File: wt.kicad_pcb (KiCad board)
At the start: 4 copper layers, 70.9 x 100 mm, 181 parts, among them J1 USB_B, J2 Conn_ARM_JTAG_SWD_10, SW1 SW_Push, SW2 SW_Push, SW3 SW_Push, SW4 SW_Push, SW5 SW_Push, SW6 SW_Push, U1 LM324, U10 LUM-1502-03_3.5mm_mono_vertic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, U11 LUM-1502-03_3.5mm_mono_vertic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, U12 LUM-1502-03_3.5mm_mono_vertic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, U13 LUM-1502-03_3.5mm_mono_vertic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, U14 LUM-1502-03_3.5mm_mono_vertic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, U15 LUM-1502-03_3.5mm_mono_vertic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, U16 power_conn_10, U17 REF191, U18 L78L05ACU, U19 ZLDO1117G33TA, U2 LM324, U20 TL072, U21 LUM-1502-03_3.5mm_mono_vertic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, U22 LUM-1502-03_3.5mm_mono_vertic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, U23 LUM-1502-03_3.5mm_mono_vertic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, U24 LUM-1502-03_3.5mm_mono_vertic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, U3 LM324, U4 STM32F407VGTx, U5 TL074, U6 TL074, U7 TLC7528, U8 LUM-1502-03_3.5mm_mono_vertic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, U9 LUM-1502-03_3.5mm_mono_vertic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, Y1 Crystal_8Mhz

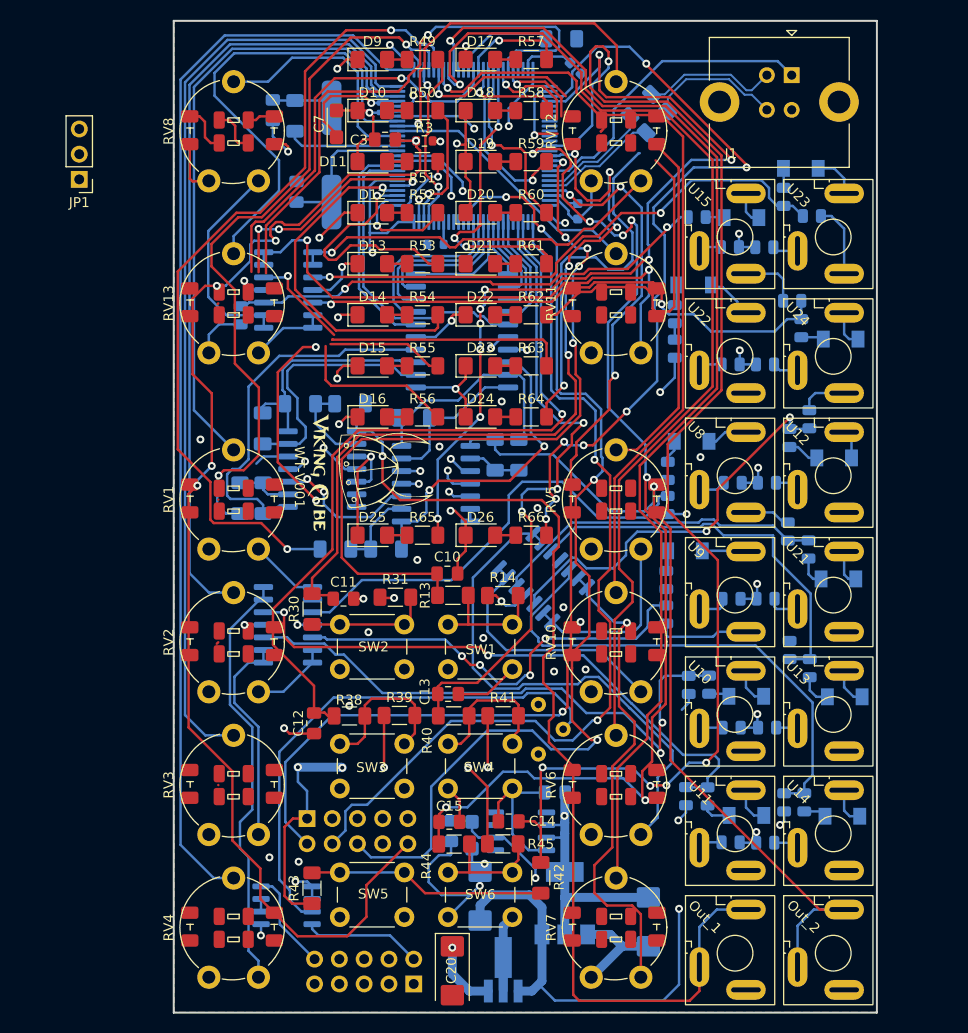
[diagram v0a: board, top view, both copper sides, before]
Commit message: fixed issues, power still needs to be addressed
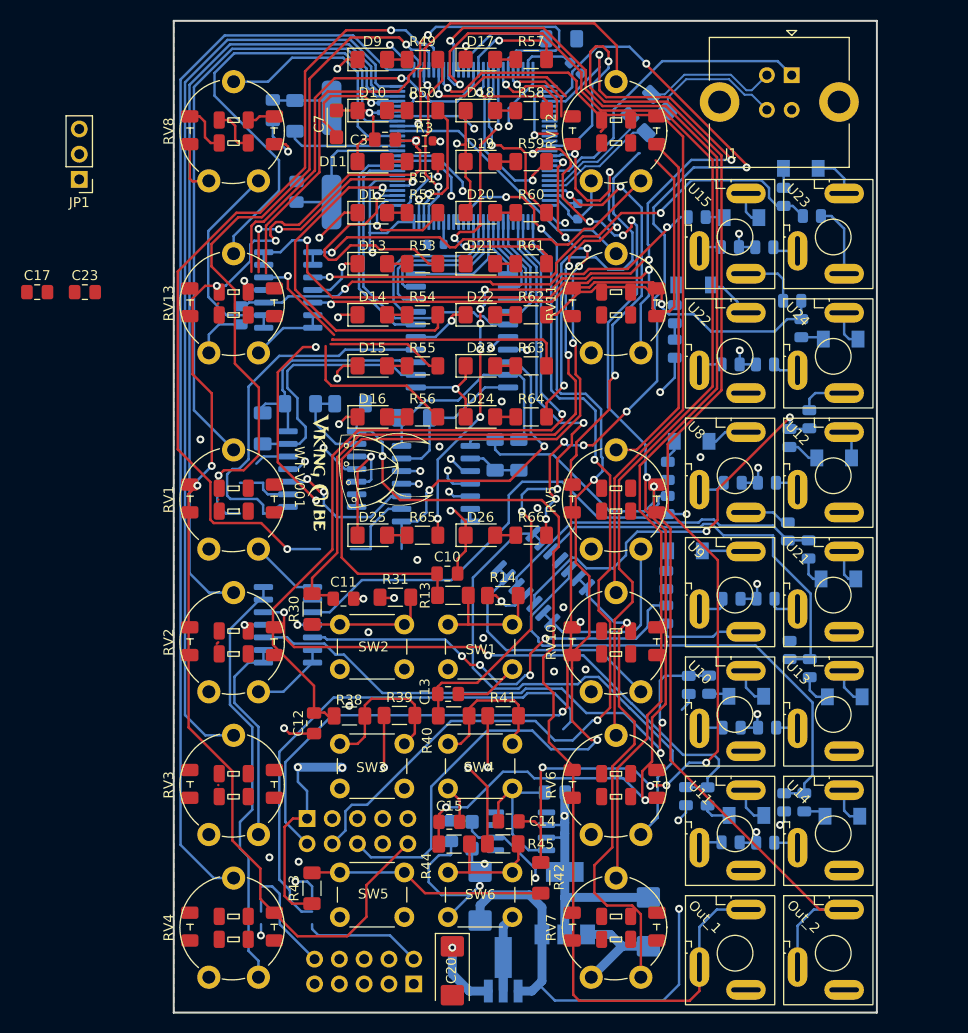
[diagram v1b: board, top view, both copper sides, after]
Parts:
- removed R5, R6, R7, R8: R-10k-1206, Resistor_SMD:R_1206_3216Metric_Pad1.30x1.75mm_HandSolder
- removed RV9: Trim_5k_prec_tht, eurorack:trim_2.5mm
- removed U20: TL072, Package_SO:SO-8_3.9x4.9mm_P1.27mm
- added C17: C-100nF-0805, Capacitor_SMD:C_0805_2012Metric_Pad1.18x1.45mm_HandSolder, F.Cu at (-13.8, 27.4)
- added C23: C-100nF-0805, Capacitor_SMD:C_0805_2012Metric_Pad1.18x1.45mm_HandSolder, F.Cu at (-8.96, 27.4)
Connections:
- R10 pad 1: Net-(C8-Pad2) -> Net-(R10-Pad1)
- R9 pad 1: Net-(C9-Pad1) -> Net-(R9-Pad1)
- U5 pad 10: -1V65 -> /DCA/InA
- U5 pad 8: Net-(R7-Pad2) -> Net-(U5-Pad8)
- U5 pad 9: Net-(R5-Pad2) -> Net-(U5-Pad8)
- U6 pad 10: -1V65 -> /DCA/InB
- U6 pad 8: Net-(R8-Pad2) -> Net-(U6-Pad8)
- U6 pad 9: Net-(R6-Pad2) -> Net-(U6-Pad8)
- U7 pad 18: Net-(R8-Pad2) -> Net-(U6-Pad8)
- U7 pad 4: Net-(R7-Pad2) -> Net-(U5-Pad8)
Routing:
- net Net-(RV11-Pad1): track 0.00 -> 142.0 mm, vias 0 -> 4
- net Net-(R79-Pad2): track 142.0 -> 0.00 mm, vias 4 -> 0
- net -1V65: track 60.7 -> 0.00 mm, vias 3 -> 0
- net /DCA/InA: track 72.1 -> 132.9 mm, vias 2 -> 5
- net (no net): track 0.00 -> 54.2 mm
- net Net-(RV9-Pad2): track 52.9 -> 0.00 mm
- net Net-(U5-Pad8): track 0.00 -> 44.1 mm
- net Net-(U6-Pad8): track 0.00 -> 39.2 mm, vias 0 -> 2
- net Net-(R7-Pad2): track 38.4 -> 0.00 mm
- net AIN4: track 52.3 -> 16.9 mm
- net GND: track 1274.1 -> 1309.5 mm
- net Net-(R8-Pad2): track 31.1 -> 0.00 mm, vias 2 -> 0
- net Net-(R6-Pad2): track 8.14 -> 0.00 mm
- net Net-(R5-Pad2): track 5.72 -> 0.00 mm
- net Net-(U20-Pad6): track 1.27 -> 0.00 mm

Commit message: New design
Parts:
- added C24: C-Pol-10uF-TAN, Capacitor_Tantalum_SMD:CP_EIA-6032-28_Kemet-C, B.Cu at (19.9, 88.2)
- added C25: C-Pol-10uF-TAN, Capacitor_Tantalum_SMD:CP_EIA-6032-28_Kemet-C, B.Cu at (30.9, 88.3)
- added JP2: Jumper_2_Open, Jumper:SolderJumper-2_P1.3mm_Open_Pad1.0x1.5mm, F.Cu at (76.4, 89.6)
- C17, C23, JP1: moved to B.Cu
- U16: value power_conn_10 -> power_conn_16; footprint eurorack:power_10 -> eurorack:power_16
- U18: value L78L05ACU -> LM7805_TO220; footprint Package_TO_SOT_SMD:SOT-89-3_Handsoldering -> Package_TO_SOT_THT:TO-220-3_Vertical
- moved JP1 53.5 mm to (43.8, 20.0), turned to -90 degrees
- moved C17 51.3 mm to (35.9, 40.2), turned to 180 degrees
- moved U18 32.2 mm to (13.3, 70.4), turned to -90 degrees
- moved C23 19.9 mm to (8.23, 37.4)
- moved C21 19.8 mm to (11.2, 90.1), turned to 180 degrees
- moved C20 9.07 mm to (37.2, 95.9)
- moved U16 7.74 mm to (31.9, 97.1)
- moved C2 6.50 mm to (12.4, 15.1)
- moved C12 5.38 mm to (14.0, 65.5), turned to 90 degrees
- moved C1 2.02 mm to (12.4, 19.3), turned to -90 degrees
- moved C22 1.54 mm to (47.0, 92.1), turned to 180 degrees
- moved R3 1.16 mm to (26.4, 12.1)
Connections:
- U18 pad 1: +5V -> +12V
- U18 pad 3: +12V -> Net-(JP2-Pad1)
- U4 pad 31: AIN4 -> AIN7
- U4 pad 32: AIN5 -> AIN6
- U4 pad 33: AIN6 -> AIN5
- U4 pad 34: AIN7 -> AIN4
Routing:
- net GND: track 1309.5 -> 1.83 mm, vias 54 -> 0
- net +3V3: track 339.5 -> 26.5 mm, vias 18 -> 0
- net +12V: track 267.0 -> 7.27 mm, vias 9 -> 0
- net /DCA/OutB: track 311.9 -> 71.7 mm, vias 9 -> 0
- net Net-(RV12-Pad10): track 181.4 -> 0.00 mm, vias 2 -> 0
- net Net-(RV11-Pad1): track 142.0 -> 0.00 mm, vias 4 -> 0
- net BTN2: track 137.4 -> 0.00 mm, vias 3 -> 0
- net /DCA/InA: track 132.9 -> 0.00 mm, vias 5 -> 0
- net BTN4: track 131.6 -> 0.00 mm, vias 5 -> 0
- net RST: track 125.4 -> 4.88 mm, vias 5 -> 1
- net 1V25: track 125.1 -> 5.82 mm, vias 4 -> 0
- net AIN7: track 0.00 -> 115.2 mm, vias 0 -> 1
- net -12V: track 110.8 -> 6.81 mm, vias 2 -> 0
- net AIN6: track 0.00 -> 100.0 mm, vias 0 -> 1
- net SWDCLK: track 91.1 -> 0.00 mm, vias 2 -> 0
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
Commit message: New design
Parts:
- JP2: moved to B.Cu
- moved JP2 66.3 mm to (10.2, 86.2), turned to -90 degrees
- moved R48 2.29 mm to (6.73, 27.4), turned to 90 degrees
- moved C6 0.62 mm to (20.3, 8.41), turned to 180 degrees
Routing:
- net /DCA/InB: track 0.00 -> 98.5 mm, vias 0 -> 2
- net /DCA/InA: track 0.00 -> 75.5 mm, vias 0 -> 2
- net /DCA/CS: track 0.00 -> 32.9 mm
- net LED6: track 0.00 -> 27.0 mm, vias 0 -> 1
- net /DCA/DACA/B: track 0.00 -> 24.9 mm
- net LED5: track 0.00 -> 22.1 mm, vias 0 -> 1
- net LED0: track 0.00 -> 17.0 mm, vias 0 -> 1
- net LED4: track 0.00 -> 14.1 mm, vias 0 -> 1
- net LED1: track 0.00 -> 12.0 mm, vias 0 -> 1
- net Net-(JP2-Pad1): track 0.00 -> 11.4 mm
- net /DCA/OutA: track 82.0 -> 91.8 mm
- net /DCA/OutB: track 71.7 -> 81.4 mm
- net AIN11: track 32.2 -> 22.9 mm, vias 0 -> 1
- net LED2: track 0.00 -> 6.91 mm, vias 0 -> 1
- net AIN0: track 60.5 -> 54.5 mm
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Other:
- board text added: "WT-V002"
- board text removed: "WT-V001"

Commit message: working on the new pcb
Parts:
- R1: moved to F.Cu
- moved R1 5.76 mm to (28.0, 17.0), turned to 180 degrees
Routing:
- net AIN3-LED: track 0.00 -> 91.4 mm, vias 0 -> 3
- net AIN6-LED: track 0.00 -> 85.6 mm, vias 0 -> 5
- net AIN4-LED: track 0.00 -> 46.9 mm, vias 0 -> 3
- net /D7: track 0.00 -> 18.1 mm
- net /D6: track 0.00 -> 16.7 mm
- net /D5: track 0.00 -> 15.3 mm
- net /D0: track 0.00 -> 12.5 mm
- net /D4: track 0.00 -> 12.0 mm
- net /D1: track 0.00 -> 11.0 mm
- net /D2: track 0.00 -> 9.25 mm
- net /D3: track 0.00 -> 6.47 mm
- net Net-(JP1-Pad2): track 24.2 -> 19.4 mm
- net Net-(R1-Pad2): track 2.26 -> 4.15 mm, vias 0 -> 1
- net LED5: track 22.1 -> 22.9 mm
- net LED6: track 27.0 -> 27.8 mm
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
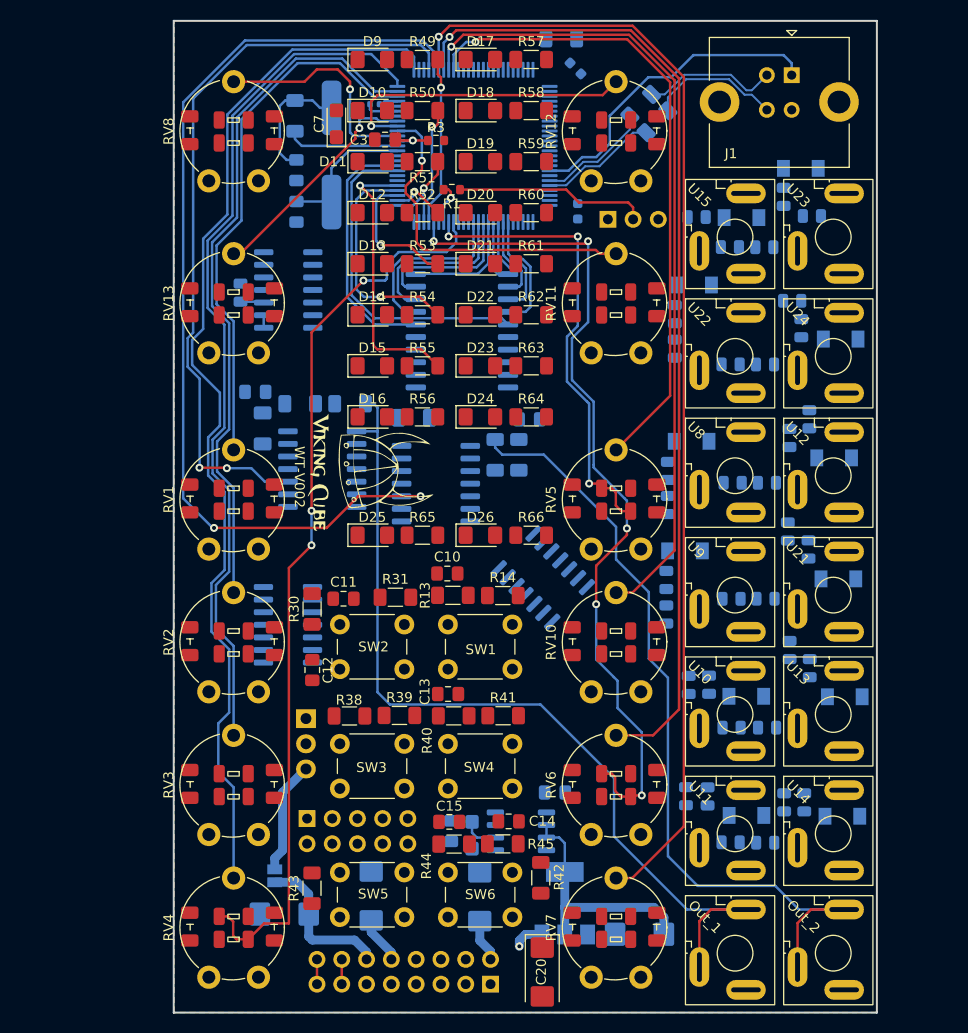
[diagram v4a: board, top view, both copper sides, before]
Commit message: working on PCB v2 LEDs
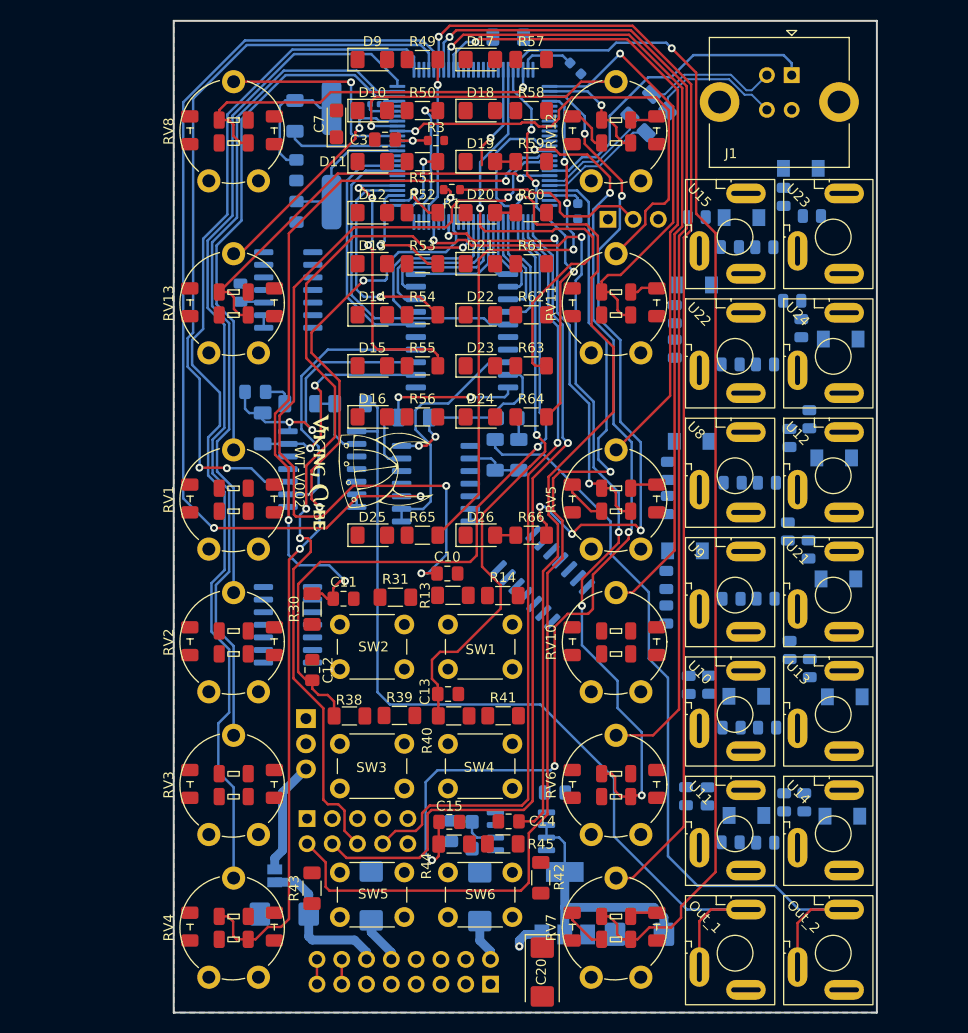
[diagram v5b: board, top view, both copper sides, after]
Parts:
- moved R4 5.35 mm to (33.7, 1.65)
- moved C17 2.11 mm to (33.8, 40.1), turned to 0 degrees
- turned C8 to 0 degrees
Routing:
- net AIN7-LED: track 0.00 -> 118.8 mm, vias 0 -> 1
- net SWDIO: track 0.00 -> 107.9 mm, vias 0 -> 1
- net BTN5: track 0.00 -> 102.6 mm, vias 0 -> 5
- net BTN4: track 0.00 -> 90.6 mm, vias 0 -> 1
- net SWDCLK: track 0.00 -> 86.6 mm, vias 0 -> 1
- net BTN1: track 0.00 -> 85.6 mm, vias 0 -> 3
- net TRACESWO: track 0.00 -> 85.1 mm, vias 0 -> 3
- net JTDI: track 0.00 -> 77.9 mm, vias 0 -> 1
- net BTN0: track 0.00 -> 75.2 mm, vias 0 -> 3
- net BTN2: track 0.00 -> 72.4 mm, vias 0 -> 1
- net LED16: track 0.00 -> 65.5 mm, vias 0 -> 5
- net BTN3: track 0.00 -> 58.5 mm, vias 0 -> 1
- net LED17: track 0.00 -> 56.0 mm, vias 0 -> 3
- net LED14: track 0.00 -> 46.6 mm, vias 0 -> 1
- net AIN11-LED: track 0.00 -> 43.2 mm, vias 0 -> 1
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
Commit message: using power plane as signal too - will this fly?
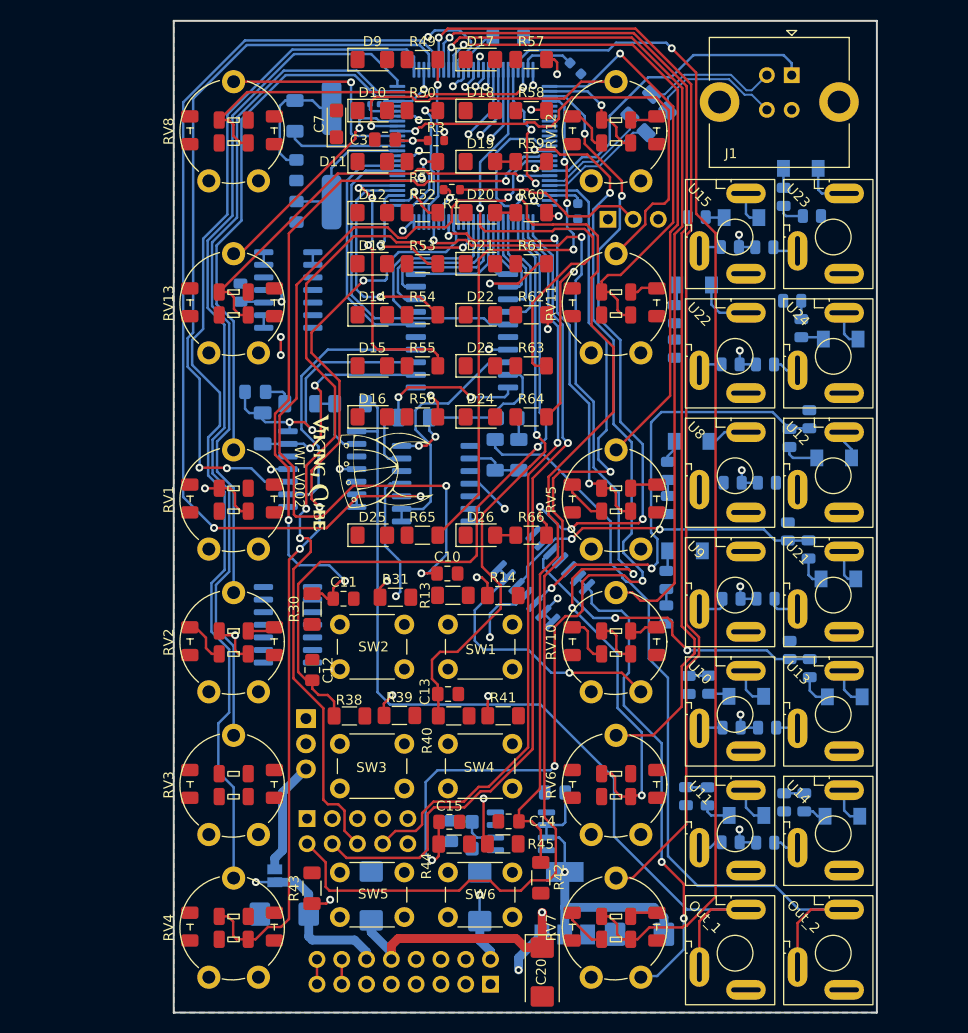
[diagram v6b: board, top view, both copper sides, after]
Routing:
- net +3V3: track 26.6 -> 351.4 mm, vias 0 -> 17
- net +12V: track 7.27 -> 256.9 mm, vias 0 -> 9
- net +5V: track 43.1 -> 123.2 mm, vias 1 -> 3
- net AIN1-LED: track 0.00 -> 78.6 mm, vias 0 -> 4
- net -12V: track 6.81 -> 85.1 mm, vias 0 -> 3
- net AIN0-LED: track 0.00 -> 75.1 mm, vias 0 -> 2
- net LED7: track 0.00 -> 64.2 mm, vias 0 -> 2
- net Net-(RV7-Pad1): track 0.00 -> 48.9 mm, vias 0 -> 2
- net Net-(R28-Pad2): track 0.00 -> 46.0 mm, vias 0 -> 2
- net Net-(R33-Pad2): track 0.00 -> 33.5 mm, vias 0 -> 2
- net Net-(R68-Pad2): track 0.00 -> 33.0 mm, vias 0 -> 2
- net LED12: track 0.00 -> 30.0 mm, vias 0 -> 2
- net Net-(RV10-Pad1): track 0.00 -> 27.9 mm, vias 0 -> 1
- net LED11: track 0.00 -> 27.0 mm, vias 0 -> 2
- net LED10: track 0.00 -> 20.2 mm, vias 0 -> 2
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
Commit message: Moved around a lot, I think we close to GND phase
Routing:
- net Net-(RV12-Pad1): track 1.27 -> 65.6 mm, vias 0 -> 2
- net Net-(R79-Pad2): track 1.85 -> 65.4 mm, vias 0 -> 2
- net Net-(R76-Pad2): track 2.82 -> 63.5 mm, vias 0 -> 4
- net Net-(R25-Pad2): track 2.19 -> 61.2 mm, vias 0 -> 4
- net Net-(RV11-Pad1): track 1.27 -> 56.5 mm, vias 0 -> 5
- net Net-(R16-Pad2): track 1.62 -> 54.3 mm, vias 0 -> 4
- net Net-(R73-Pad2): track 1.66 -> 54.0 mm, vias 0 -> 4
- net Net-(R22-Pad2): track 2.06 -> 50.8 mm, vias 0 -> 4
- net Net-(RV6-Pad1): track 0.00 -> 48.6 mm, vias 0 -> 1
- net Net-(R19-Pad2): track 1.66 -> 47.2 mm, vias 0 -> 4
- net Net-(RV4-Pad1): track 0.00 -> 44.0 mm
- net Net-(R36-Pad2): track 2.03 -> 42.3 mm, vias 0 -> 2
- net +3V3: track 351.4 -> 374.7 mm, vias 17 -> 18
- net Net-(RV3-Pad1): track 0.00 -> 21.1 mm
- net Net-(RV8-Pad1): track 1.27 -> 21.5 mm
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
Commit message: Getting into GND-ing
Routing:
- net 1V25: track 5.82 -> 101.8 mm, vias 0 -> 6
- net AIN2-LED: track 0.00 -> 86.0 mm, vias 0 -> 4
- net AIN5-LED: track 4.73 -> 88.8 mm, vias 0 -> 6
- net Net-(R47-Pad2): track 2.38 -> 74.2 mm, vias 0 -> 4
- net Net-(R42-Pad1): track 0.00 -> 28.0 mm, vias 0 -> 2
- net Net-(R13-Pad1): track 0.00 -> 19.4 mm, vias 0 -> 1
- net Net-(R30-Pad1): track 0.00 -> 14.5 mm, vias 0 -> 1
- net Net-(R38-Pad1): track 0.00 -> 12.6 mm
- net +3V3: track 374.7 -> 387.3 mm
- net Net-(R44-Pad1): track 0.00 -> 12.5 mm
- net Net-(R40-Pad1): track 0.00 -> 12.4 mm
- net LED7: track 68.3 -> 75.0 mm
- net Net-(RV11-Pad5): track 0.00 -> 5.31 mm
- net Net-(RV8-Pad5): track 0.00 -> 5.23 mm
- net Net-(RV6-Pad5): track 0.00 -> 5.21 mm
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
